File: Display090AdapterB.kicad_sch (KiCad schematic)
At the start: 22 parts, among them J1 FFC3B07-40-T, J15 Conn_02x05_Odd_Even, J17 Stepper Header, J2 ER-TFTM090 header, J21 Display, J3 Node I/O, J4 Bridge, J5 Home Sensor, J6 NeoPixel, J7 External Power, J8 Bridge Sensor, J9 Node I/O-3, SW1 Display Reset

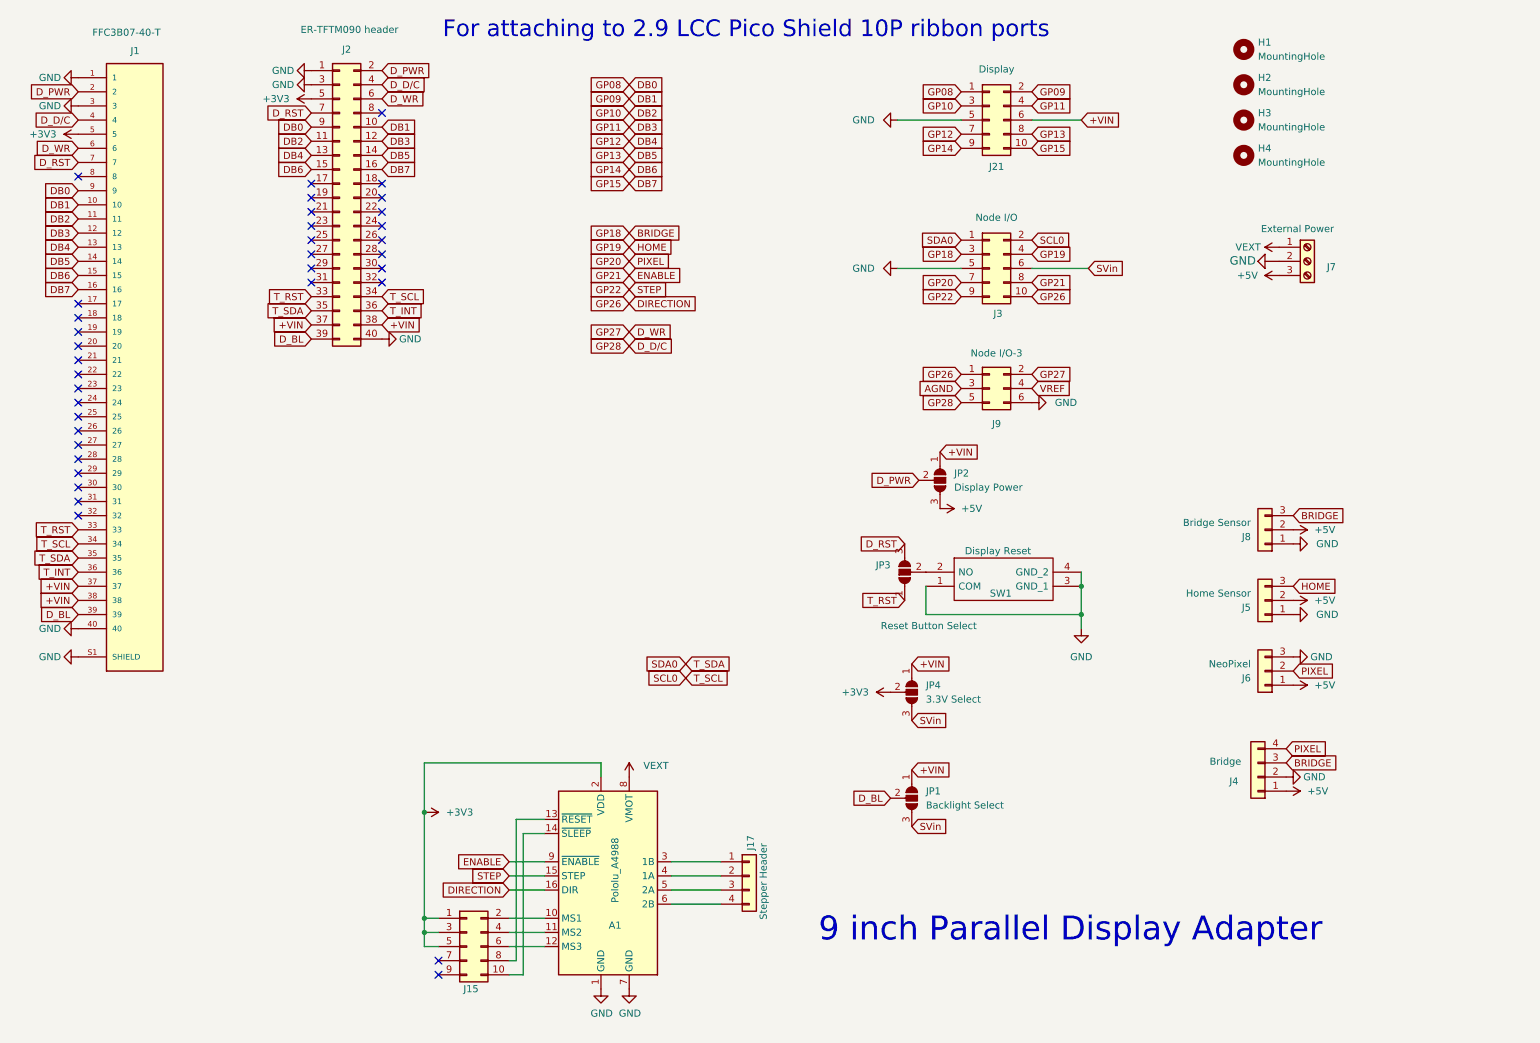
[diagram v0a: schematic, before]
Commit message: Add Display090AdapterB & update gerbers
Replace Display090Adapter with a new Display090AdapterB set (new .kicad_pcb/.kicad_pro and updated .kicad_prl/.kicad_sch). Update RibbonBreakout and RibbonBreakout2 board files. Remove many individual gerber output files and add consolidated GERBER-*.zip archives under gerbers/. Also remove temporary/backup documentation files. These changes package gerbers and introduce the B revision of the 090 adapter.
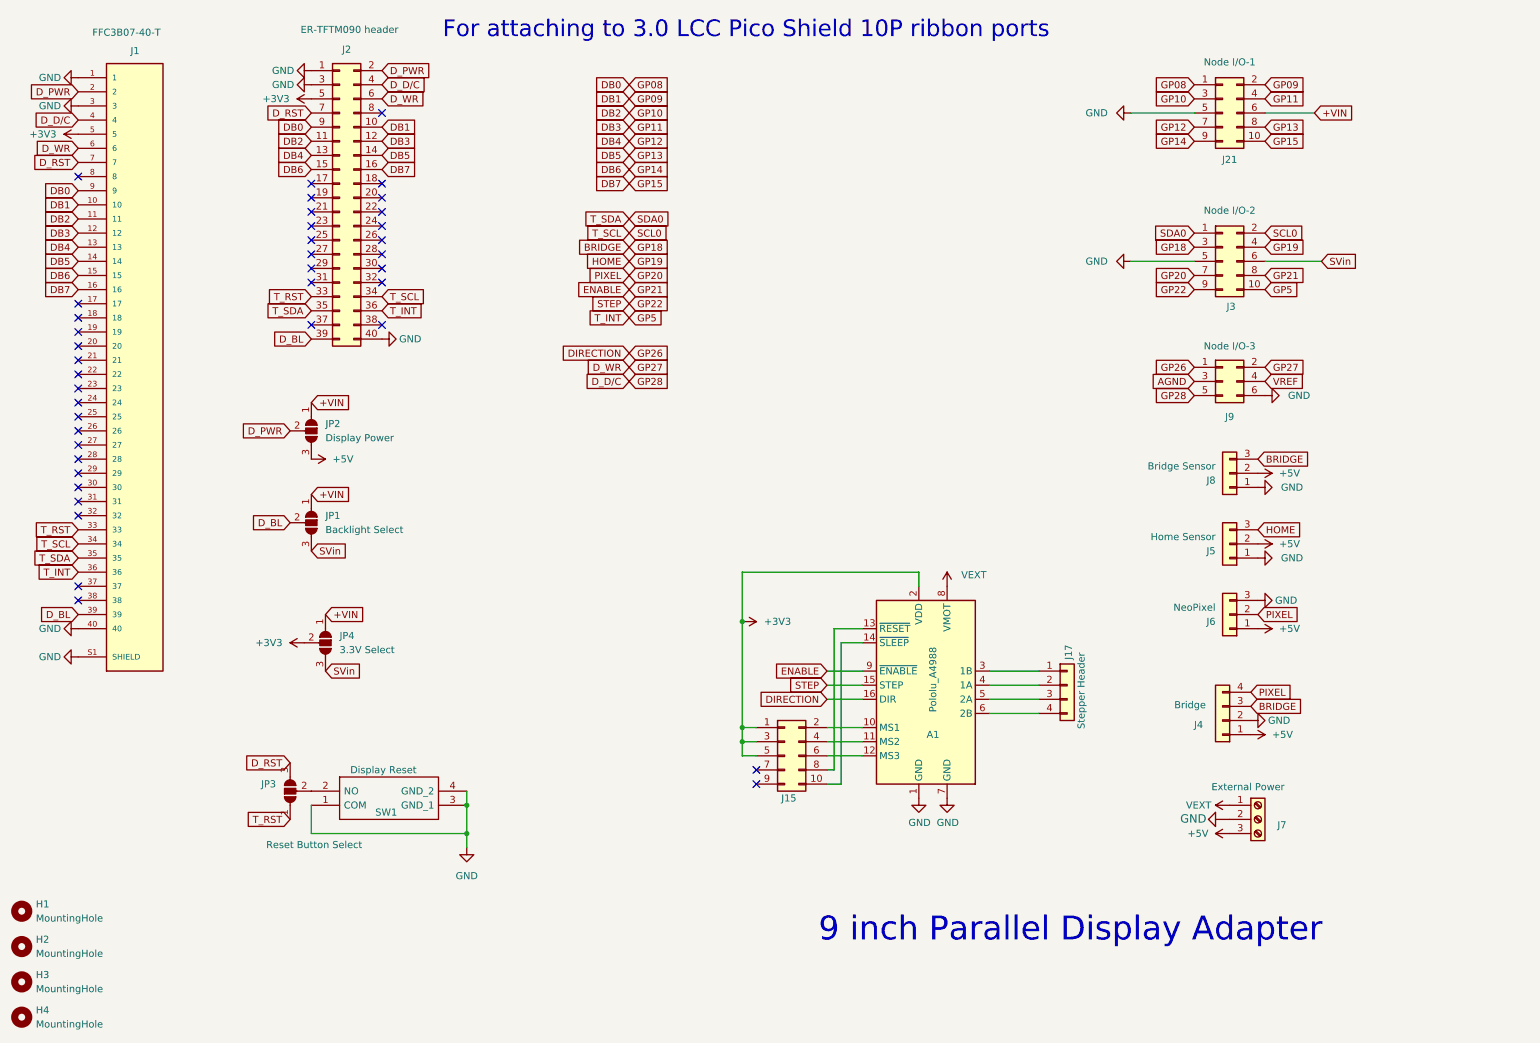
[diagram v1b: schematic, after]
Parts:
- J21: value Display -> Node I/O-1
- J3: value Node I/O -> Node I/O-2
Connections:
- net +VIN: no longer J1.37, J1.38, J2.37 (Pin_37), J2.38 (Pin_38)
- net DIRECTION: no longer J3.10 (Pin_10)
- net T_INT renamed GP5
- net GP5: now also J3.10 (Pin_10)
- no-connect marks 36 -> 40
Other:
- note added: "For attaching to 3.0 LCC Pico Shield 10P ribbon ports"
- note removed: "For attaching to 2.9 LCC Pico Shield 10P ribbon ports"
- moved on the sheet: A1, H1, H2, H3, H4, J15, J17, J21, J3, J4, J5, J6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
